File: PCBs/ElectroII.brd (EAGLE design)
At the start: 114.3 x 76.2 mm, 40 parts, among them J1 U.FL-R-SMT(01), T1 VIN, T2 VBAT, T3 GND, T4 BOOST, T5 VCC, T6 5V, U1 RFM95W-868S2, U2 TPS61090RSAR

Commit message: more board shuffling
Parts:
- removed CR1: DIODE_SB340-E3/54, DIODE_SB340-E3-54:DIODE_DO-201AD
- added D2: 1N4004, adafruit:DO41-10
- R1: value 2M -> 1.96M
- moved BRK0 85.4 mm to (58.4, 54.6)
- moved R9 82.4 mm to (7.62, 26.7)
- moved T6 81.5 mm to (31.8, 31.8)
- moved I2C1_BRK 69.6 mm to (38.1, 54.6)
- moved UART0_BRK 59.7 mm to (43.2, 54.6), turned to 0 degrees
- moved T1 47.0 mm to (3.81, 58.4)
- moved SPI1_BRK 43.7 mm to (53.3, 54.6)
- moved T2 36.9 mm to (8.26, 48.3)
- moved SPI0_BRK 36.1 mm to (48.3, 54.6), turned to 0 degrees
- moved SPI0 27.9 mm to (74.9, 76.2)
- moved R8 27.5 mm to (39.4, 38.1), turned to 180 degrees
- moved T4 24.7 mm to (17.1, 35.6)
- moved I2C1 24.1 mm to (48.3, 76.2)
- moved R7 19.9 mm to (39.4, 41.9), turned to 180 degrees
- moved R3 9.16 mm to (17.1, 55.9)
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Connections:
- net 5V: now also D2.C; no longer CR1.1
- net BOOST_OUT: now also D2.A; no longer CR1.2
- net GND: now also U2.PGND1, U2.PGND2, U2.PGND3, U2.PGND4; no longer U2.P$1, U2.P$2, U2.P$3, U2.P$4
- net VBAT: now also CN1.1, F1.1, T1.P$1; no longer C3.1, D1.C, F1.2, L1.P$1, R3.2, T2.P$1, U2.11, U2.8
- net VIN: now also C3.1, D1.C, F1.2, L1.P$1, R3.2, T2.P$1, U2.11, U2.8; no longer CN1.1, F1.1, T1.P$1
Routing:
- net VCC: track 0.00 -> 246.0 mm, vias 0 -> 2
- net 5V: track 0.00 -> 196.5 mm, vias 0 -> 4
- net MOSI: track 0.00 -> 99.7 mm, vias 0 -> 2
- net MISO: track 0.00 -> 98.3 mm, vias 0 -> 2
- net SCLK: track 0.00 -> 92.6 mm, vias 0 -> 4
- net SCL: track 0.00 -> 89.7 mm, vias 0 -> 1
- net SDA: track 0.00 -> 81.0 mm, vias 0 -> 1
- net CE1: track 0.00 -> 69.8 mm
- net I2C1_GPIO2: track 0.00 -> 69.6 mm, vias 0 -> 1
- net N$22: track 0.00 -> 68.3 mm
- net GPIO21: track 0.00 -> 68.0 mm
- net CE0: track 0.00 -> 63.8 mm
- net UART0_GPIO3: track 0.00 -> 61.2 mm, vias 0 -> 2
- net UART0_GPIO1: track 0.00 -> 59.4 mm
- net N$45: track 0.00 -> 58.8 mm
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
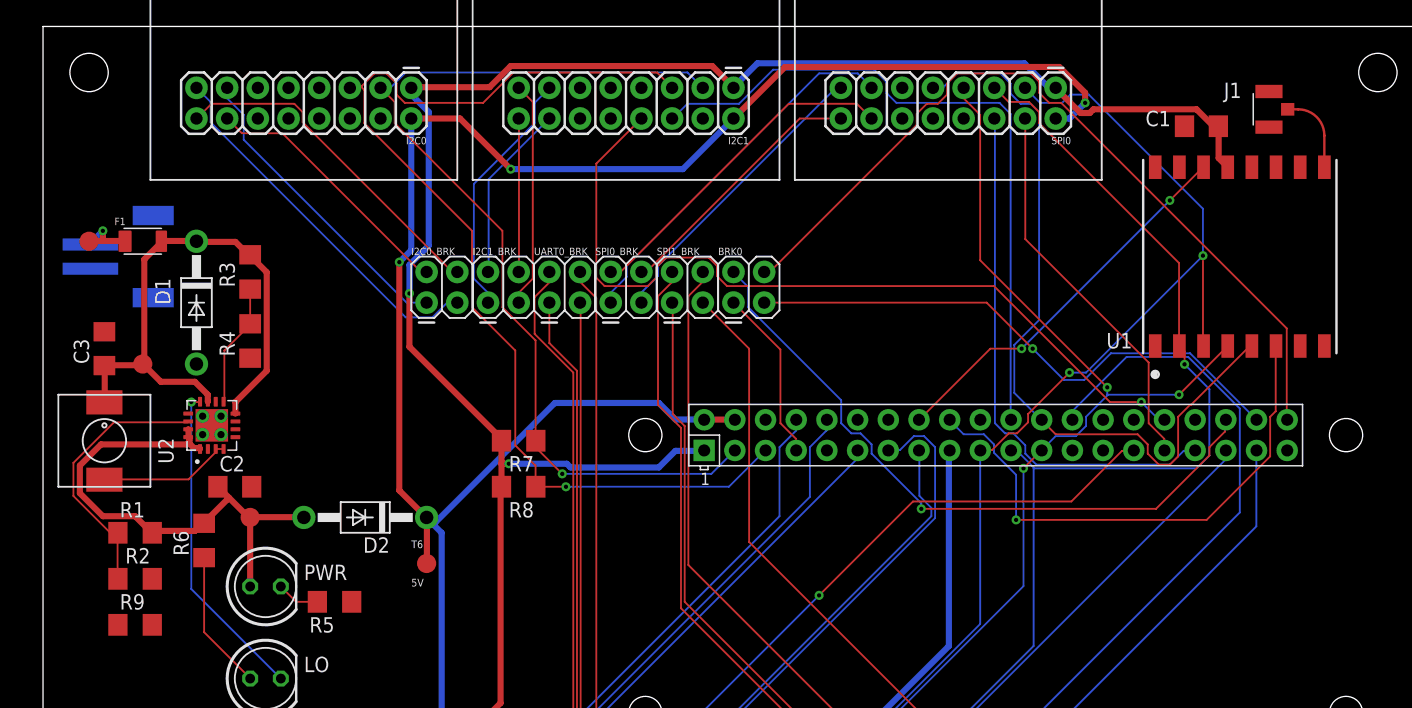
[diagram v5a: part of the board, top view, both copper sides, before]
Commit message: Reviewed traces and fixed joints
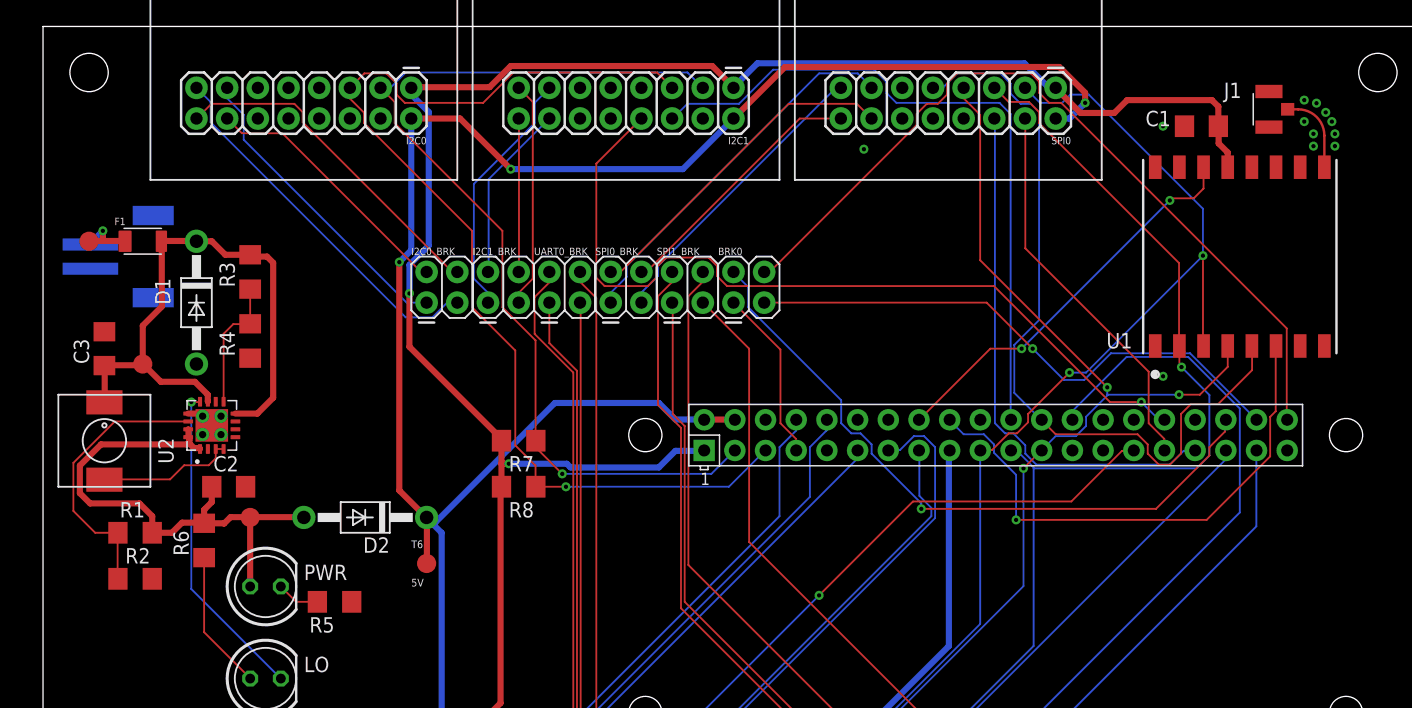
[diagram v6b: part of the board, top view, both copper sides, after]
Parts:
- removed R9: 0.1 1/8w, RTR Main Library:R1206
- moved C2 0.51 mm to (15.4, 38.1)
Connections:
- removed net CGND: R9.1
- net GND: no longer R9.2
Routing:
- net VIN: track 46.6 -> 49.0 mm
- net VCC: track 246.0 -> 247.7 mm
- net BOOST_OUT: track 43.2 -> 44.8 mm
- net CE0: track 63.8 -> 65.2 mm
- net GND: track 1.08 -> 2.36 mm, vias 0 -> 12
- net SCLK: track 92.6 -> 93.7 mm
- net SPI2_GPIO1: track 32.2 -> 33.3 mm
- net LBI: track 10.2 -> 11.0 mm
- net FB: track 22.5 -> 23.2 mm
- net MISO: track 98.3 -> 98.9 mm
- net N$4: track 11.1 -> 11.6 mm
